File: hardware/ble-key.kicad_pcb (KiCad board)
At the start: 2 copper layers, 46 x 26 mm, 39 parts, among them J1 USB4105-GF-A, J2 SJ-3523-SMT, J3 JST PH battery, J4 SWD, SW1 reset, U1 MDBT50Q-1MV2, U2 BQ24074RGTR, U3 USBLC6-2SC6, Y1 32.768k

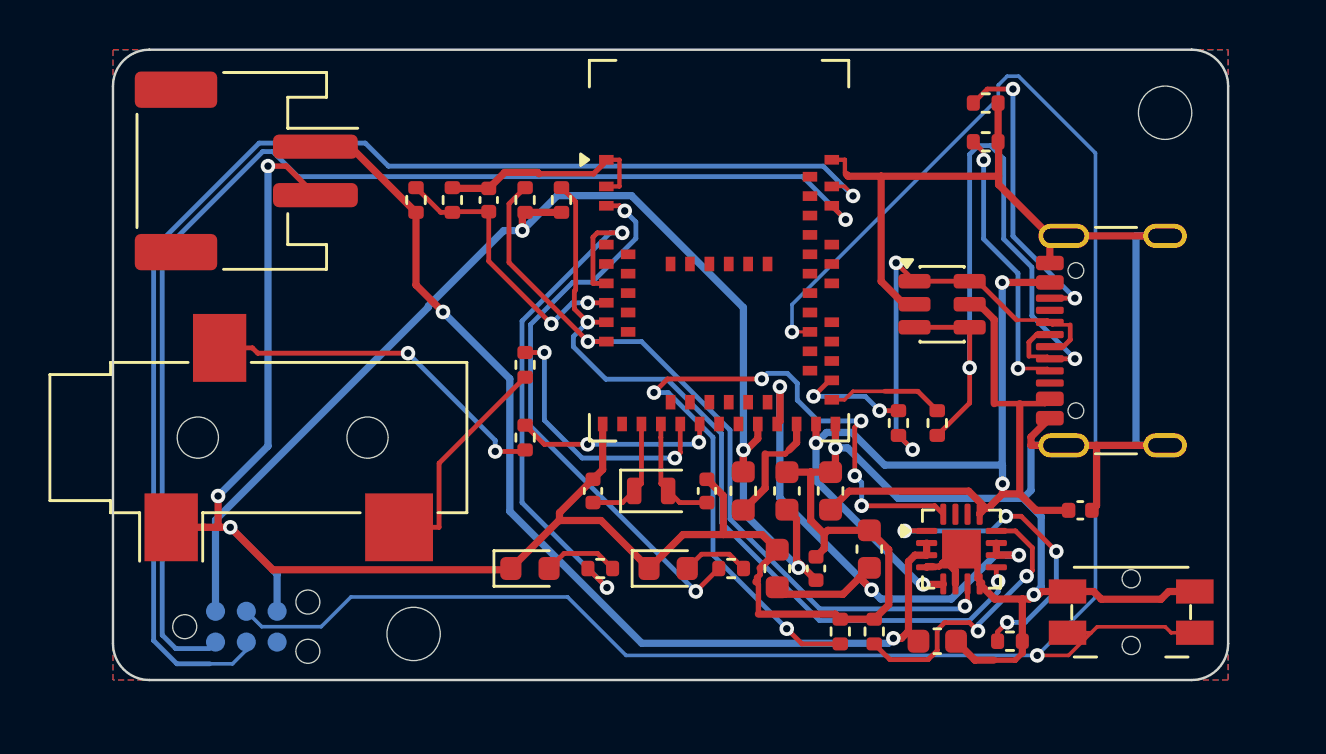
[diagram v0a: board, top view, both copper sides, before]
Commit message: fix: stitch the board's ground pours and give the charger room
Ground is routed first so every pad has a real connection, then a grid of
stitching vias ties the two pours together and extra vias join patches that
traces cut off. The charger's exposed pad gets thermal vias and the ESD chip a
ground dog-bone. The board grows to 48 x 27 mm so the charger corner can be
routed. DRC: no errors, no unconnected pads.

Co-Authored-By: Claude Opus 5.5 <noreply@anthropic.com>
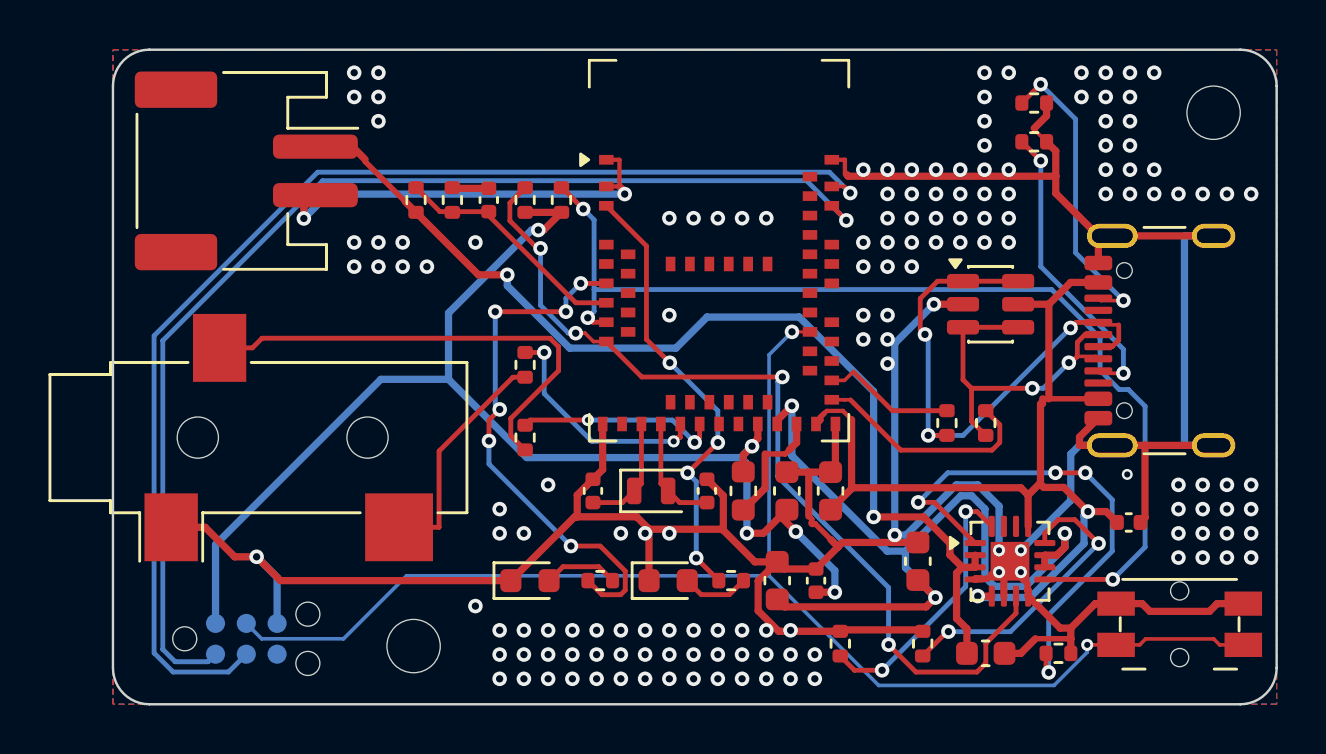
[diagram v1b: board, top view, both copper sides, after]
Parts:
- moved C1 2.06 mm to (141.9, 119.5)
- moved C2 2.06 mm to (133.2, 121.1)
- moved C3 2.06 mm to (136.0, 124.9)
- moved R3 2.06 mm to (139.0, 124.9)
- moved R4 2.06 mm to (133.4, 124.5)
- moved SW1 2.06 mm to (144.0, 123.7)
- moved U2 2.06 mm to (137.0, 121.1)
- moved H1 2.00 mm to (145.4, 102.6)
- moved J1 2.00 mm to (144.3, 112.0)
- moved R1 2.00 mm to (138.0, 103.8)
- moved R14 2.00 mm to (134.4, 115.4)
- moved R15 2.00 mm to (136.0, 115.4)
- moved R2 2.00 mm to (138.0, 102.2)
- moved U3 2.00 mm to (136.2, 110.5)
- moved C5 0.50 mm to (127.4, 121.9)
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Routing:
- net ~{RESET}: track 84.1 -> 56.6 mm
- net ISET: track 32.1 -> 11.3 mm, vias 6 -> 2
- net USB_DN_C: track 30.9 -> 14.5 mm
- net VBUS: track 50.6 -> 40.0 mm, vias 4 -> 2
- net ~{CHG}: track 33.9 -> 42.9 mm, vias 2 -> 3
- net VSYS: track 25.0 -> 33.6 mm
- net TS: track 13.2 -> 21.1 mm
- net ~{PGOOD}: track 32.0 -> 37.8 mm, vias 2 -> 4
- net JACK_R: track 14.7 -> 19.6 mm, vias 2 -> 0
- net LED_BLUE: track 23.2 -> 18.4 mm, vias 2 -> 4
- net USB_DN: track 4.83 -> 9.47 mm
- net USB_DP_C: track 18.6 -> 22.3 mm, vias 2 -> 3
- net SWDCLK: track 53.6 -> 50.3 mm
- net SWDIO: track 50.2 -> 47.7 mm
- net VBAT_SENSE: track 11.8 -> 10.1 mm, vias 2 -> 0
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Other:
- board size 46 x 26 mm -> 48 x 27 mm

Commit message: feat: printable case for the nRF52840 board, USB-only and with battery
board_case.py builds a base and a lid around the custom board from the
board's exported STEP and mechanics.json: two M2 x 8 screws clamp the board
between them, the lid arches over USB-C and the jack, a flexible tongue
reaches the reset switch and a light channel carries the status LEDs. The
battery version holds the LP-552035 in a lid pocket above the board.

The board changes to fit: the JST plug points inward, the LEDs move to the
top-right corner, and one mounting hole and the SWD pads move out from under
the cell. The preview page shows all four cases.

Co-Authored-By: Claude Opus 5.5 <noreply@anthropic.com>
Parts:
- moved D1 30.1 mm to (141.0, 103.4)
- moved D2 24.6 mm to (141.0, 105.2)
- moved R12 22.5 mm to (135.6, 105.6)
- moved R13 18.0 mm to (135.6, 107.0)
- moved H2 3.07 mm to (109.5, 125.6)
- moved C4 2.80 mm to (115.5, 109.0)
- moved R6 2.80 mm to (117.0, 109.0)
- moved R7 2.80 mm to (118.5, 109.0)
- moved R8 2.80 mm to (112.5, 109.0)
- moved R9 2.80 mm to (114.0, 109.0)
- moved J4 1.58 mm to (104.0, 123.8)
- turned J3 to 90 degrees
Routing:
- net VBAT: track 43.4 -> 60.3 mm, vias 2 -> 3
- net TS: track 21.1 -> 8.90 mm, vias 4 -> 2
- net ~{CHG}: track 42.9 -> 33.1 mm
- net CC1: track 12.4 -> 20.4 mm
- net SWDIO: track 47.7 -> 40.0 mm, vias 1 -> 3
- net SWDCLK: track 50.3 -> 42.7 mm, vias 1 -> 3
- net ~{RESET}: track 56.6 -> 62.4 mm, vias 2 -> 3
- net JACK_R: track 19.6 -> 14.3 mm, vias 0 -> 2
- net LED_B_A: track 2.80 -> 8.03 mm, vias 0 -> 2
- net VSYS: track 33.6 -> 28.5 mm, vias 3 -> 5
- net LED_R_A: track 3.10 -> 6.59 mm
- net LED_RED: track 22.0 -> 18.6 mm, vias 6 -> 2
- net USB_DN: track 9.47 -> 7.09 mm, vias 0 -> 2
- net LED_BLUE: track 18.4 -> 16.2 mm, vias 4 -> 2
- net VBUS: track 40.0 -> 42.1 mm
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
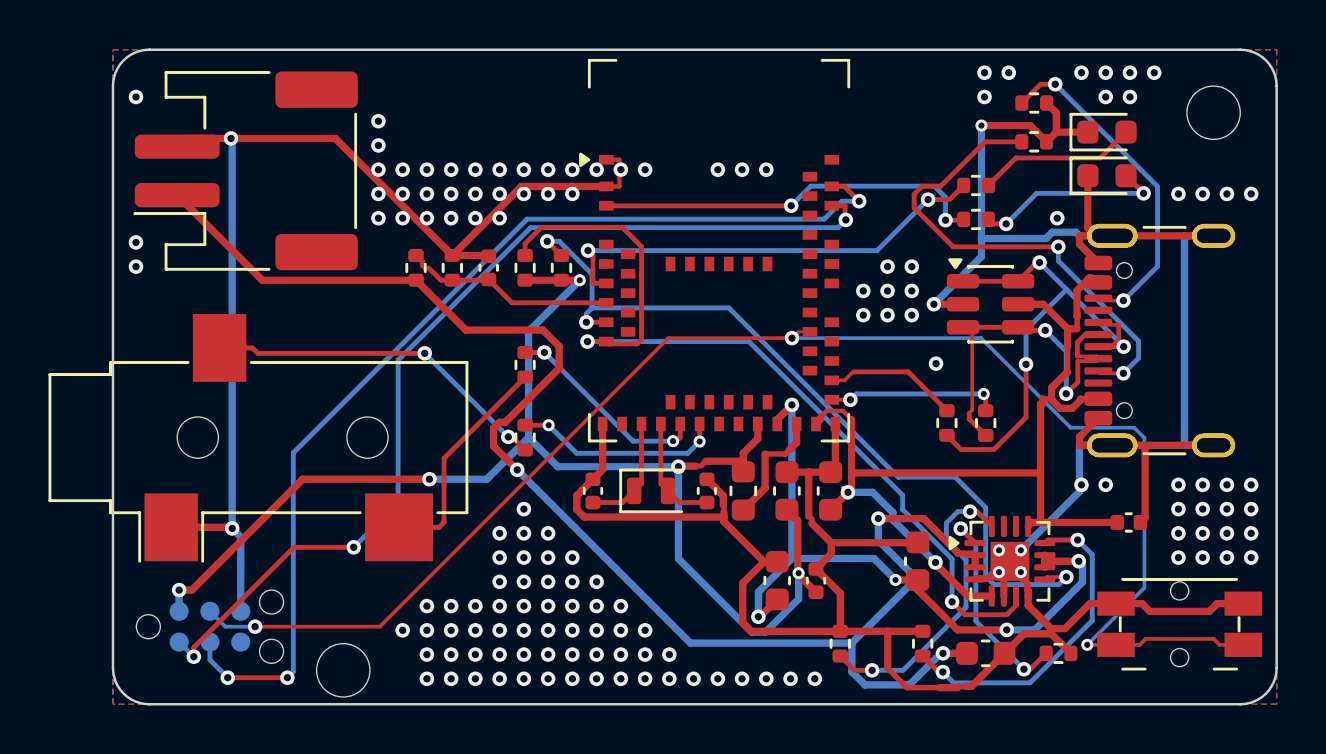
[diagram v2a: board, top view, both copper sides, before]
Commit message: feat: part numbers for the crystal, its capacitors and the DC/DC inductor
Y1 Epson FC-12M (CL 9 pF, matched to the 12 pF capacitors per Nordic's
guidance), C9/C10 Murata GRM1555C1H120GA01D, L1 Taiyo Yuden LBMF1608T100K as
on the nRF52840-DK. The board's footprints now carry the MPN field too, so
AISLER can match parts from the layout file.

Co-Authored-By: Claude Opus 5.5 <noreply@anthropic.com>
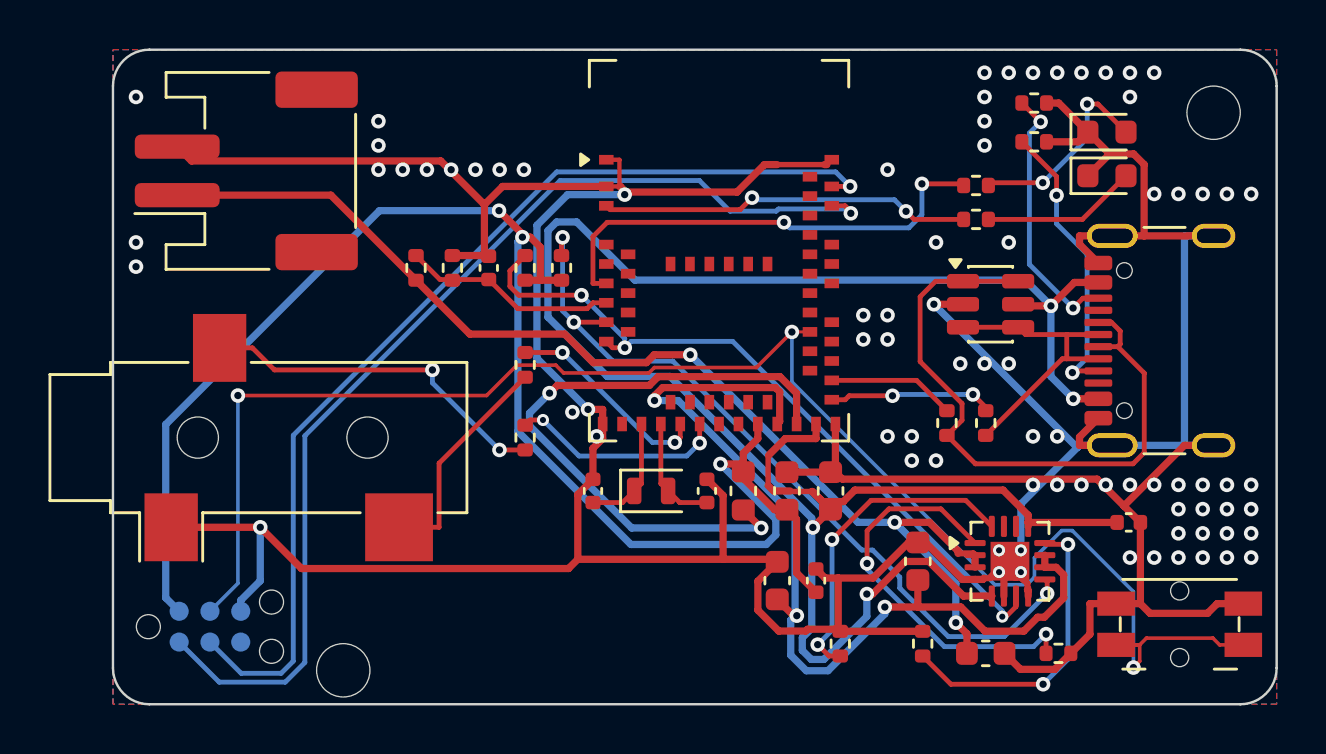
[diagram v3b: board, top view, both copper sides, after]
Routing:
- net VBUS: track 42.1 -> 87.5 mm, vias 2 -> 4
- net GND: track 173.9 -> 202.6 mm, vias 145 -> 79
- net DCCH: track 4.94 -> 26.1 mm, vias 0 -> 2
- net VBAT: track 60.3 -> 46.5 mm
- net VSYS: track 28.5 -> 38.9 mm, vias 5 -> 3
- net VDD: track 54.7 -> 65.0 mm, vias 5 -> 3
- net CC1: track 20.4 -> 12.0 mm
- net TS: track 8.90 -> 16.7 mm
- net ~{PGOOD}: track 36.3 -> 30.1 mm, vias 2 -> 3
- net USB_DP_C: track 21.4 -> 27.2 mm, vias 3 -> 0
- net ~{RESET}: track 62.4 -> 67.0 mm
- net SWDIO: track 40.0 -> 44.0 mm, vias 3 -> 1
- net USB_DN_C: track 16.1 -> 12.7 mm, vias 2 -> 0
- net CC2: track 14.0 -> 10.9 mm
- net LED_R_A: track 6.59 -> 8.38 mm, vias 0 -> 2
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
